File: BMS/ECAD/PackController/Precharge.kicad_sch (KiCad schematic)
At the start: 32 parts, among them K1 KT12-1A-40L-THT, Q6 IRLML0100TR, Q7 IXTA08N100D2HV, Q8 BC846, Q9 DMP4065S-7, U7 TCLT1004, U8 TCLT1004, U9 TEA1-0505HI

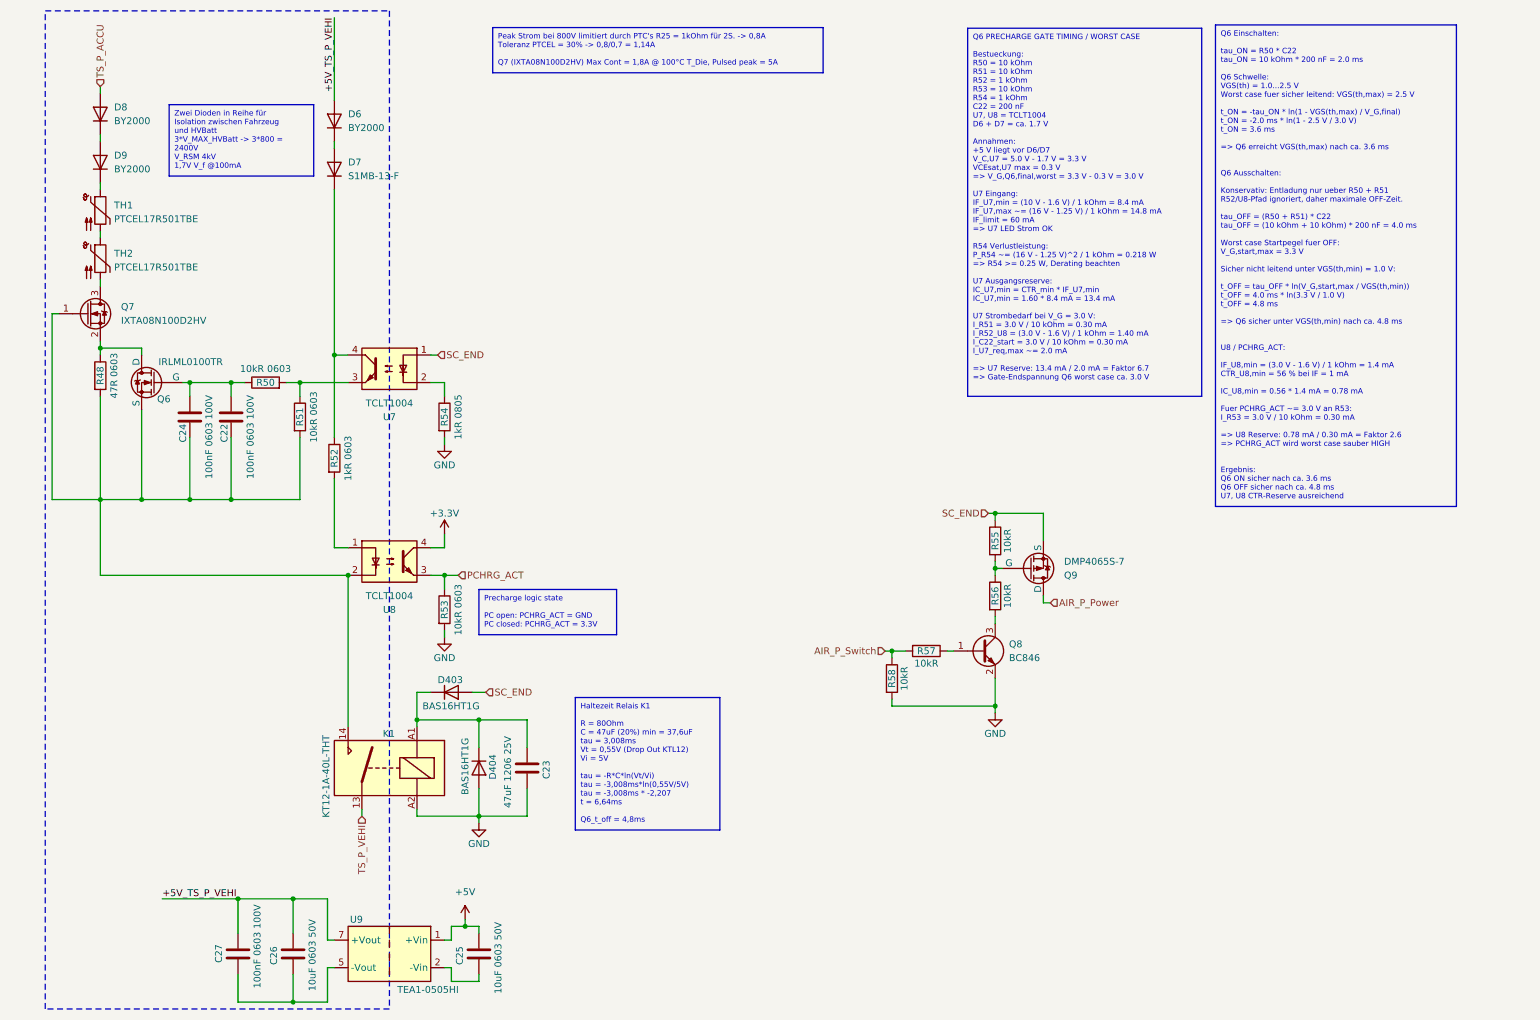
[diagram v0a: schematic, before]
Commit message: implement HV measurement
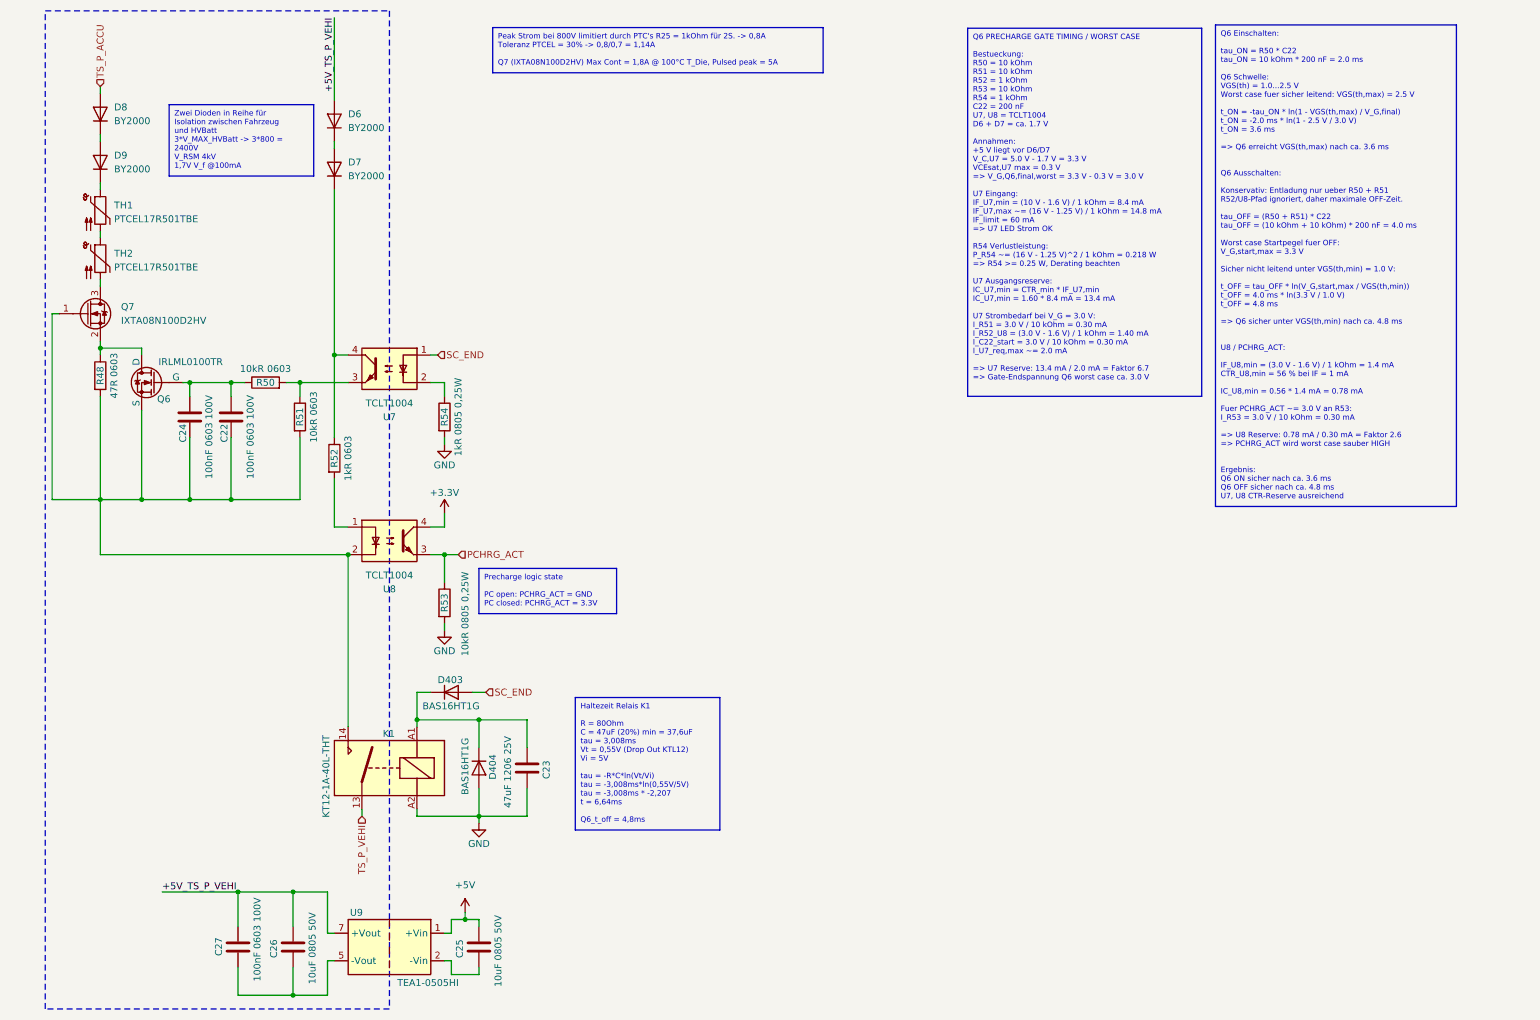
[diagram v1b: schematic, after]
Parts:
- removed Q8: BC846, Package_TO_SOT_SMD:SOT-23, symbol Transistor_BJT:BC846
- removed Q9: DMP4065S-7, Package_TO_SOT_SMD:SOT-23-3, symbol Simulation_SPICE:PMOS
- removed R55, R56, R57, R58: 10kR, Resistor_SMD:R_0603_1608Metric_Pad0.98x0.95mm_HandSolder, symbol Device:R
- C25, C26: value 10uF 0603 50V -> 10uF 0805 50V; footprint Capacitor_SMD:C_0603_1608Metric_Pad1.08x0.95mm_HandSolder -> Capacitor_SMD:C_0805_2012Metric
- D7: value S1MB-13-F -> BY2000; footprint Diode_SMD:D_SMB -> Diode_THT:D_DO-201AE_P12.70mm_Horizontal
- R53: value 10kR 0603 -> 10kR 0805 0,25W; footprint Resistor_SMD:R_0603_1608Metric_Pad0.98x0.95mm_HandSolder -> Resistor_SMD:R_0805_2012Metric
- R54: value 1kR 0805 -> 1kR 0805 0,25W; footprint Resistor_SMD:R_0603_1608Metric_Pad0.98x0.95mm_HandSolder -> Resistor_SMD:R_0805_2012Metric
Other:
- moved on the sheet: C25, C26, C27, R53, U8, U9

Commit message: schematic finished, review tbd
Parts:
- added Q405: DMP4065S-7, Package_TO_SOT_SMD:SOT-23-3, symbol Transistor_FET:Q_PMOS_GSD
- added Q8: BC846, Package_TO_SOT_SMD:SOT-23, symbol Transistor_BJT:BC846
- added R423, R425, R426: 10kR, Resistor_SMD:R_0603_1608Metric, symbol Device:R
- added R424: 4k7R, Resistor_SMD:R_0603_1608Metric, symbol Device:R
- added R78, R80: 9.09M 0.1%, Resistor_SMD:R_0603_1608Metric_Pad0.98x0.95mm_HandSolder, symbol Device:R
- added R81, R83: 1M 0.1%, Resistor_SMD:R_0603_1608Metric_Pad0.98x0.95mm_HandSolder, symbol Device:R
- added R84: 10kR, Resistor_SMD:R_0603_1608Metric_Pad0.98x0.95mm_HandSolder, symbol Device:R
- added U14: (no value), symbol EKartParts:ADCMP393ARUZ
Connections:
- net +3.3V: now also R84.1
- net GND: now also Q8.2 (E), R423.2, R78.2, R80.2
- net SC_END: now also Q405.2 (S), R425.1; no longer D403.2 (A), U7.1
- net PCHRG_ACT renamed PCHRG_ACTUAL
- new net: R80.1, R83.2, U14.11 (+)
- new net: R78.1, R81.2, U14.8 (-)
- new net: Q405.1 (G), R425.2, R426.1
- new net: Q8.1 (B), R424.1
- new net: Q8.3 (C), R426.2
- new net PCHRG_Enable: D403.2 (A), Q405.3 (D), U7.1
- new net PCHRG_SWITCH: R423.1, R424.2
- new net PRCHG_DONE: U14.14
- new net V_ACCU: R81.1, R83.1
- new net V_VEHI: U14.10 (-), U14.9 (+)
- new net nPRCHG_DONE: R84.2, U14.13

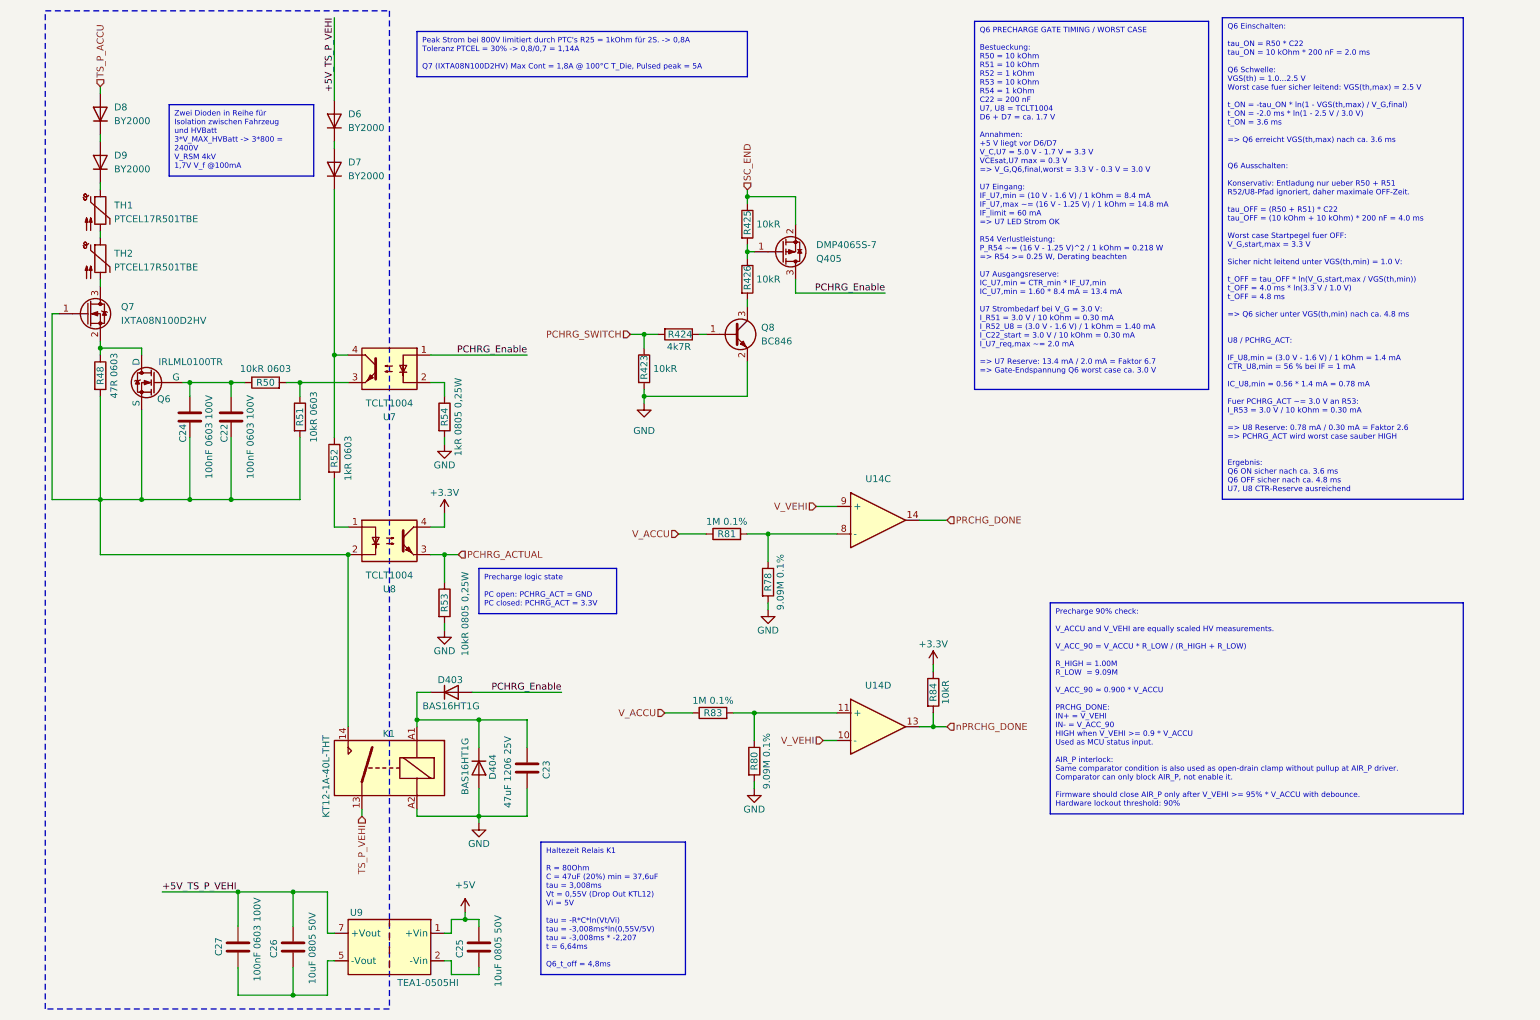
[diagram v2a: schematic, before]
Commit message: close to finish BMS master, only some footprints needed
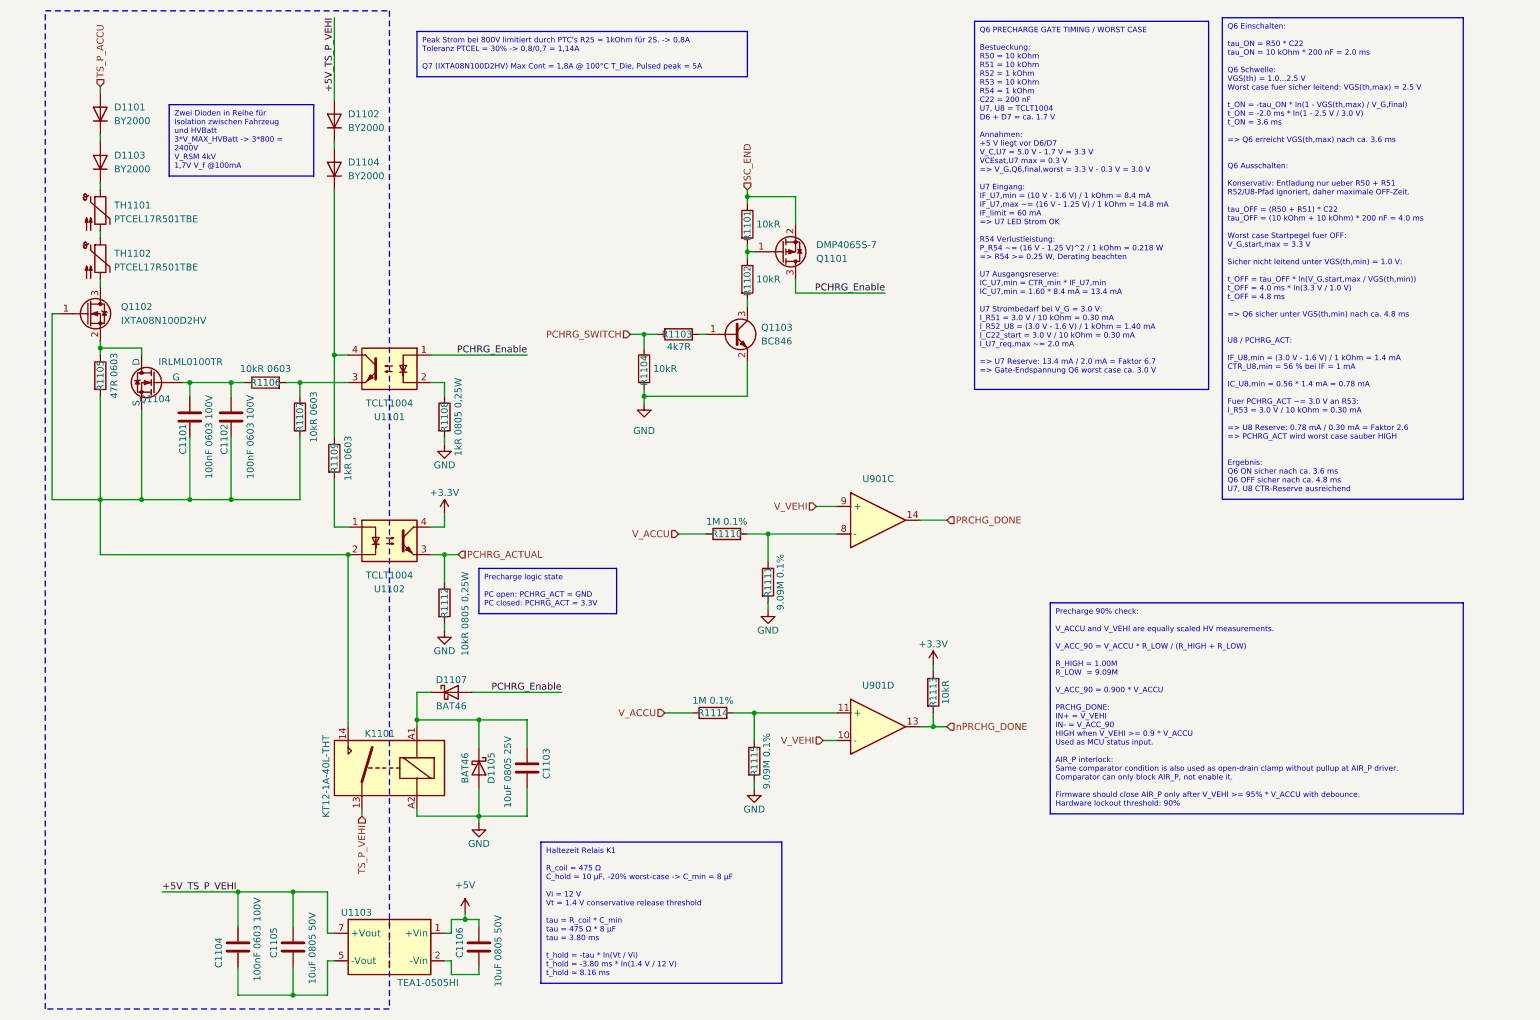
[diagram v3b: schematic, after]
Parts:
- removed D403, D404: BAS16HT1G, Diode_SMD:D_SOD-323F, symbol Device:D
- added D1105, D1107: BAT46, Diode_SMD:D_SOD-123, symbol Diode:BAT46
- C1103: renamed from C23; value 47uF 1206 25V -> 10uF 0805 25V; footprint Capacitor_SMD:C_0603_1608Metric_Pad1.08x0.95mm_HandSolder -> Capacitor_SMD:C_0805_2012Metric
- renumbered C24 to C1101, C22 to C1102, C27 to C1104, C26 to C1105, C25 to C1106, D8 to D1101, D6 to D1102, D9 to D1103, D7 to D1104, K1 to K1101, Q405 to Q1101, Q7 to Q1102, Q8 to Q1103, Q6 to Q1104, R425 to R1101, R426 to R1102, R424 to R1103, R423 to R1104, R48 to R1105, R50 to R1106, R51 to R1107, R54 to R1108, R52 to R1109, R81 to R1110, R78 to R1111, R53 to R1112, R84 to R1113, R83 to R1114, R80 to R1115, TH1 to TH1101, TH2 to TH1102, U7 to U1101, U8 to U1102, U9 to U1103, U14 to U901
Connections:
- net GND: now also D1105.2 (A)
- net PCHRG_Enable: now also D1107.2 (A)
- net at C1103.1, K1101.A1: now also D1105.1 (K), D1107.1 (K)

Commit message: finalised schematic of pack controller
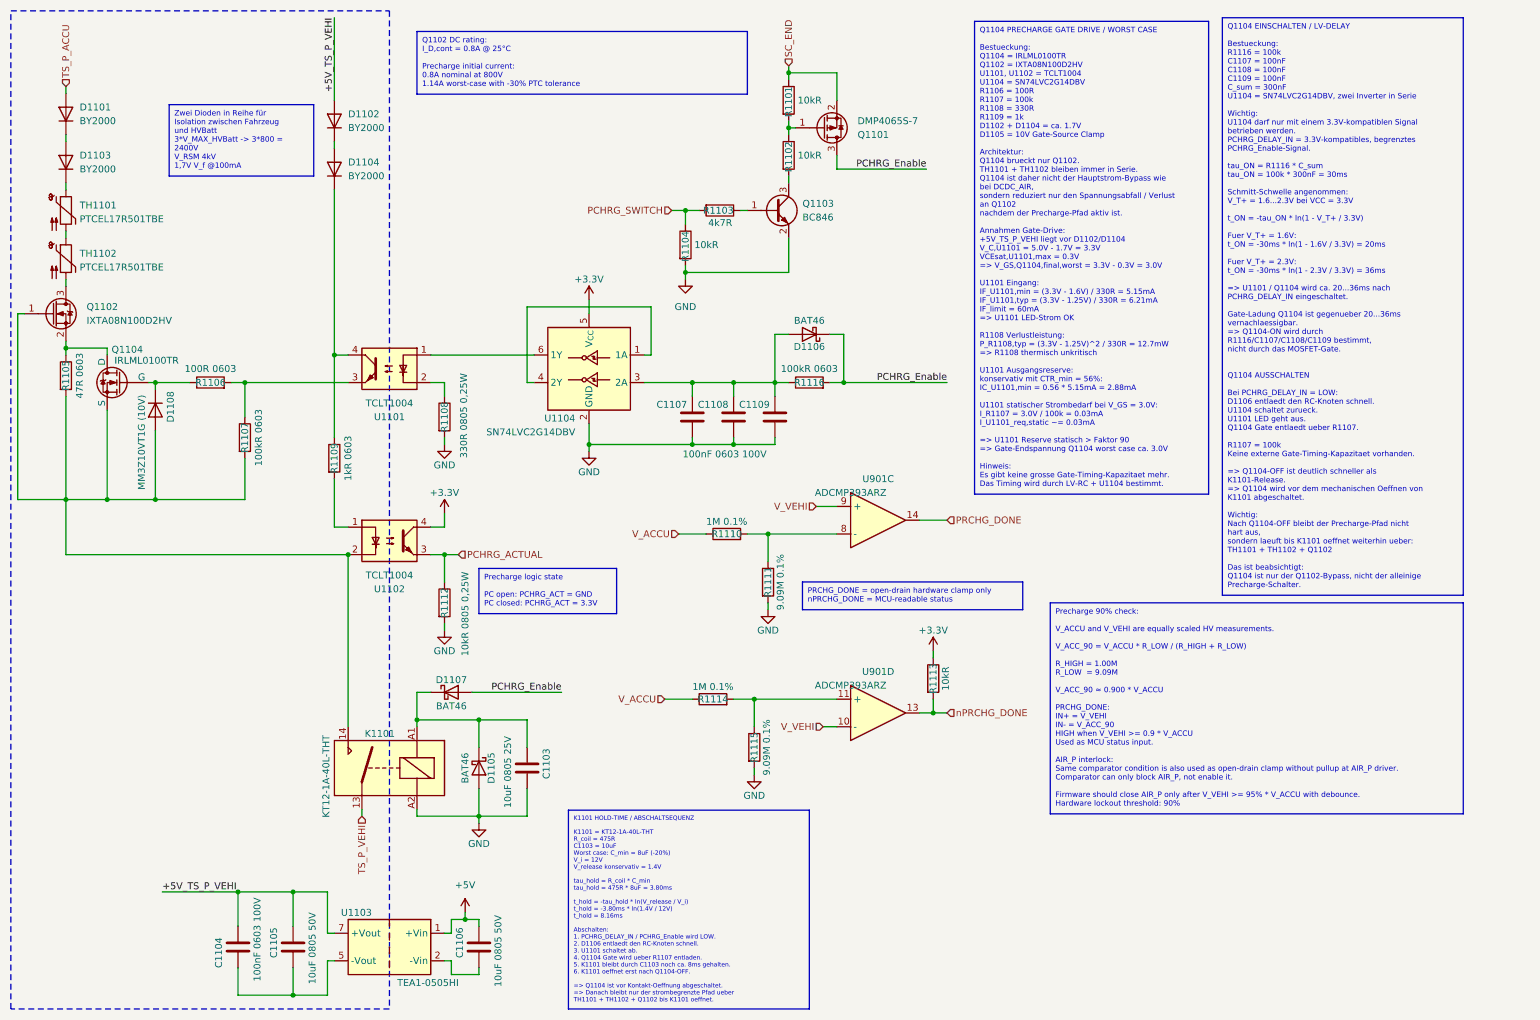
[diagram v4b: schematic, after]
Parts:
- removed C1101, C1102: 100nF 0603 100V, Capacitor_SMD:C_0603_1608Metric_Pad1.08x0.95mm_HandSolder, symbol Device:C
- added C1107, C1108, C1109: 100nF 0603 100V, Capacitor_SMD:C_0603_1608Metric_Pad1.08x0.95mm_HandSolder, symbol Device:C
- added D1106: BAT46, Diode_SMD:D_SOD-123, symbol Diode:BAT46
- added D1108: MM3Z10VT1G (10V), Diode_SMD:D_SOD-323_HandSoldering, symbol Device:D
- added R1116: 100kR 0603, Resistor_SMD:R_0603_1608Metric_Pad0.98x0.95mm_HandSolder, symbol Device:R
- added U1104: SN74LVC2G14DBV, Package_TO_SOT_SMD:SOT-23-6, symbol 74xGxx:SN74LVC2G14DBV
- K1101: footprint (none) -> EKartParts:Meder_KT_Relay
- R1106: value 10kR 0603 -> 100R 0603
- R1107: value 10kR 0603 -> 100kR 0603
- R1108: value 1kR 0805 0,25W -> 330R 0805 0,25W
- U901: value (none) -> ADCMP393ARZ; footprint (none) -> Package_SO:SOIC-14_3.9x8.7mm_P1.27mm
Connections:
- net +3.3V: now also U1104.5 (V_{CC})
- net GND: now also C1107.1, C1108.1, C1109.1, U1104.2 (GND)
- net PCHRG_Enable: now also D1106.1 (K), R1116.2; no longer U1101.1
- net at K1101.14, Q1102.1 (G), Q1104.3 (S)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: now also D1108.2 (A)
- net at Q1104.2 (G), R1106.1: now also D1108.1 (K)
- new net: C1107.2, C1108.2, C1109.2, D1106.2 (A), R1116.1, U1104.3 (2A)
- new net: U1101.1, U1104.6 (1Y)
- new net: U1104.1 (1A), U1104.4 (2Y)
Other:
- moved on the sheet: D1101, D1103, Q1101, Q1102, Q1103, Q1104, R1101, R1102, R1103, R1104, R1105, R1106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

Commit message: many fixes
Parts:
- removed R1111, R1115: 9.09M 0.1%, Resistor_SMD:R_0603_1608Metric_Pad0.98x0.95mm_HandSolder, symbol Device:R
- removed R1113: 10kR, Resistor_SMD:R_0603_1608Metric_Pad0.98x0.95mm_HandSolder, symbol Device:R
- removed R1114: 1M 0.1%, Resistor_SMD:R_0603_1608Metric_Pad0.98x0.95mm_HandSolder, symbol Device:R
- removed U901: ADCMP393ARZ, Package_SO:SOIC-14_3.9x8.7mm_P1.27mm, symbol EKartParts:ADCMP393ARUZ
- R1105: footprint Resistor_SMD:R_0603_1608Metric_Pad0.98x0.95mm_HandSolder -> Resistor_SMD:R_1206_3216Metric
- R1110: value 1M 0.1% -> 500R 0805; footprint Resistor_SMD:R_0603_1608Metric_Pad0.98x0.95mm_HandSolder -> Resistor_SMD:R_0805_2012Metric_Pad1.20x1.40mm_HandSolder
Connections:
- net V_ACCU is gone; now on net TS_P_VEHI: R1110.1
- net +5V_TS_P_VEHI: now also R1110.2
- net TS_P_VEHI: now also C1104.1, C1105.2, U1103.5 (-Vout)
